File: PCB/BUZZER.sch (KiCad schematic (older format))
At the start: 3 parts

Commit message: Annotated Schematic
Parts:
- gave numbers to parts that had none: 3
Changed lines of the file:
@@
 $EndDescr
 $Comp
-L Device:Buzzer BZ?
+L Device:Buzzer BZ1
 U 1 1 5E8EB805
 P 5600 4000
-F 0 "BZ?" H 5752 4029 50  0000 L CNN
+F 0 "BZ1" H 5752 4029 50  0000 L CNN
 F 1 "Buzzer" H 5752 3938 50  0000 L CNN
 F 2 "" V 5575 4100 50  0001 C CNN
-F 3 "~" V 5575 4100 50  0001 C CNN
+F 3 "" V 5575 4100 50  0001 C CNN
 	1    5600 4000
 	1    0    0    -1
 $EndComp
 $Comp
-L dk_Transistors-Bipolar-BJT-Single:MMBT4401-7-F Q?
+L dk_Transistors-Bipolar-BJT-Single:MMBT4401-7-F Q1
 U 1 1 5E8EBE2A
 P 5300 4450
-F 0 "Q?" H 5488 4503 60  0000 L CNN
+F 0 "Q1" H 5488 4503 60  0000 L CNN
 F 1 "MMBT4401-7-F" H 5488 4397 60  0000 L CNN
 F 2 "digikey-footprints:SOT-23-3" H 5500 4650 60  0001 L CNN
@@
 	5400 4100 5500 4100
 $Comp
-L power:GND #PWR?
+L power:GND #PWR053
 U 1 1 5E8EC551
 P 5400 4700
-F 0 "#PWR?" H 5400 4450 50  0001 C CNN
+F 0 "#PWR053" H 5400 4450 50  0001 C CNN
 F 1 "GND" H 5405 4527 50  0000 C CNN
 F 2 "" H 5400 4700 50  0001 C CNN
@@
 	5400 4700 5400 4650
 $Comp
-L power:+3.3V #PWR?
+L power:+3.3V #PWR052
 U 1 1 5E8EC82E
 P 5400 3800
-F 0 "#PWR?" H 5400 3650 50  0001 C CNN
+F 0 "#PWR052" H 5400 3650 50  0001 C CNN
 F 1 "+3.3V" H 5415 3973 50  0000 C CNN
 F 2 "" H 5400 3800 50  0001 C CNN
@@
 	5400 3900 5500 3900
 $Comp
-L Device:R_Small R?
+L Device:R_Small R8
 U 1 1 5E8ED016
 P 4900 4450
-F 0 "R?" V 4704 4450 50  0000 C CNN
+F 0 "R8" V 4704 4450 50  0000 C CNN
 F 1 "1k" V 4795 4450 50  0000 C CNN
 F 2 "" H 4900 4450 50  0001 C CNN
-F 3 "~" H 4900 4450 50  0001 C CNN
+F 3 "" H 4900 4450 50  0001 C CNN
 	1    4900 4450
 	0    1    1    0

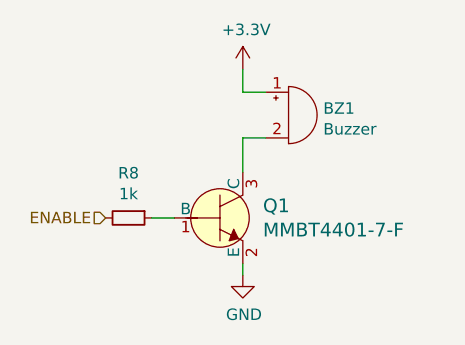
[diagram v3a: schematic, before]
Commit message: Increased VCC from 3v3 to 5v
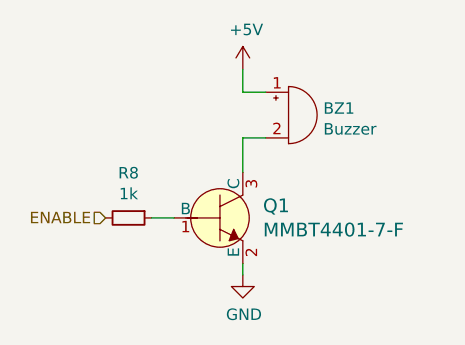
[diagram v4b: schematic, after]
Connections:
- net +3V3 renamed +5V
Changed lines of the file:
@@
 Wire Wire Line
 	5400 4700 5400 4650
-$Comp
-L power:+3.3V #PWR052
-U 1 1 5E8EC82E
-P 5400 3800
-F 0 "#PWR052" H 5400 3650 50  0001 C CNN
-F 1 "+3.3V" H 5415 3973 50  0000 C CNN
-F 2 "" H 5400 3800 50  0001 C CNN
-F 3 "" H 5400 3800 50  0001 C CNN
-	1    5400 3800
-	1    0    0    -1
-$EndComp
 Wire Wire Line
 	5400 3800 5400 3900
@@
 Text HLabel 4800 4450 0    50   Input ~ 0
 ENABLE
+$Comp
+L power:+5V #PWR?
+U 1 1 5E920954
+P 5400 3800
+F 0 "#PWR?" H 5400 3650 50  0001 C CNN
+F 1 "+5V" H 5415 3973 50  0000 C CNN
+F 2 "" H 5400 3800 50  0001 C CNN
+F 3 "" H 5400 3800 50  0001 C CNN
+	1    5400 3800
+	1    0    0    -1
+$EndComp
 $EndSCHEMATC

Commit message: Added Humidity and temperature sensors
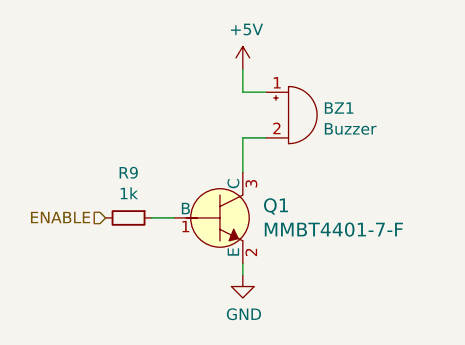
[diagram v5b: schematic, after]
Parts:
- renumbered R8 to R9
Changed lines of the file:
@@
 	5400 3900 5500 3900
 $Comp
-L Device:R_Small R8
+L Device:R_Small R9
 U 1 1 5E8ED016
 P 4900 4450
-F 0 "R8" V 4704 4450 50  0000 C CNN
+F 0 "R9" V 4704 4450 50  0000 C CNN
 F 1 "1k" V 4795 4450 50  0000 C CNN
 F 2 "" H 4900 4450 50  0001 C CNN
@@
 U 1 1 5E920954
 P 5400 3800
-F 0 "#PWR?" H 5400 3650 50  0001 C CNN
+AR Path="/5E8A6686/5E920954" Ref="#PWR?"  Part="1"
+AR Path="/5E8EB699/5E920954" Ref="#PWR052"  Part="1"
+F 0 "#PWR052" H 5400 3650 50  0001 C CNN
 F 1 "+5V" H 5415 3973 50  0000 C CNN
 F 2 "" H 5400 3800 50  0001 C CNN

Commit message: Checkpoint
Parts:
- BZ1: Voltage Rating (none) -> 5V
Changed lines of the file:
@@
 F 2 "" V 5575 4100 50  0001 C CNN
 F 3 "" V 5575 4100 50  0001 C CNN
+F 4 "5V" H 5600 4000 50  0001 C CNN "Voltage Rating"
 	1    5600 4000
 	1    0    0    -1
